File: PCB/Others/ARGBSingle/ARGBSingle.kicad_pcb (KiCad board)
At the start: 2 copper layers, 13.5 x 7 mm, 9 parts, among them J1 DIN, J2 DOUT, J3 VCC, J4 GND, J5 VCC, J6 GND

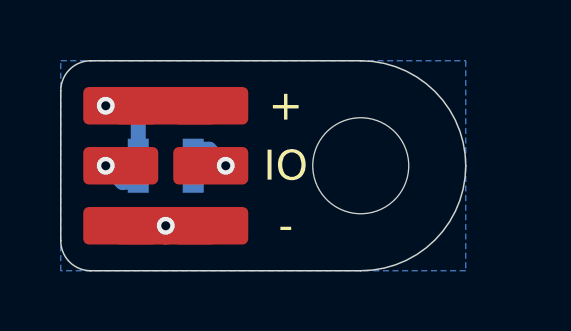
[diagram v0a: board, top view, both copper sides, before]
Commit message: feat: Rework single ARGB board, adjust screw slot, make break away.
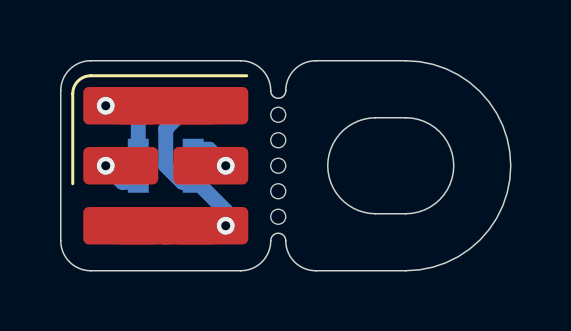
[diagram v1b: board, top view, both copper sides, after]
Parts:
- removed H1: MountingHole, KTANE:MountingHole_3.2mm_M3_NoCopper
- added REF**: BreakLine_5h_D0.5mm_P0.85mm, Panelization:BreakLine_5h_D0.5mm_P0.85mm, F.Cu at (28.2, 18.0)
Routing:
- net GND: track 3.00 -> 8.44 mm
- removed copper zone on B.Cu, net GND
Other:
- board size 13.5 x 7 mm -> 15 x 7 mm
- board text removed: "+"
- board text removed: "-"
- board text removed: "IO"
